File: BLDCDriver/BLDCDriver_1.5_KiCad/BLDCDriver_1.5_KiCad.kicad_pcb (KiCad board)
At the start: 2 copper layers, 42 x 43.2 mm, 53 parts, among them IC1 STSPIN32G4, J2 Debug, J3 Motor Out, J4 POWER, J5 CAN, SW1 SW_Push, U4 MCP2562-E-SN, U5 AS5048A-HTSP-500

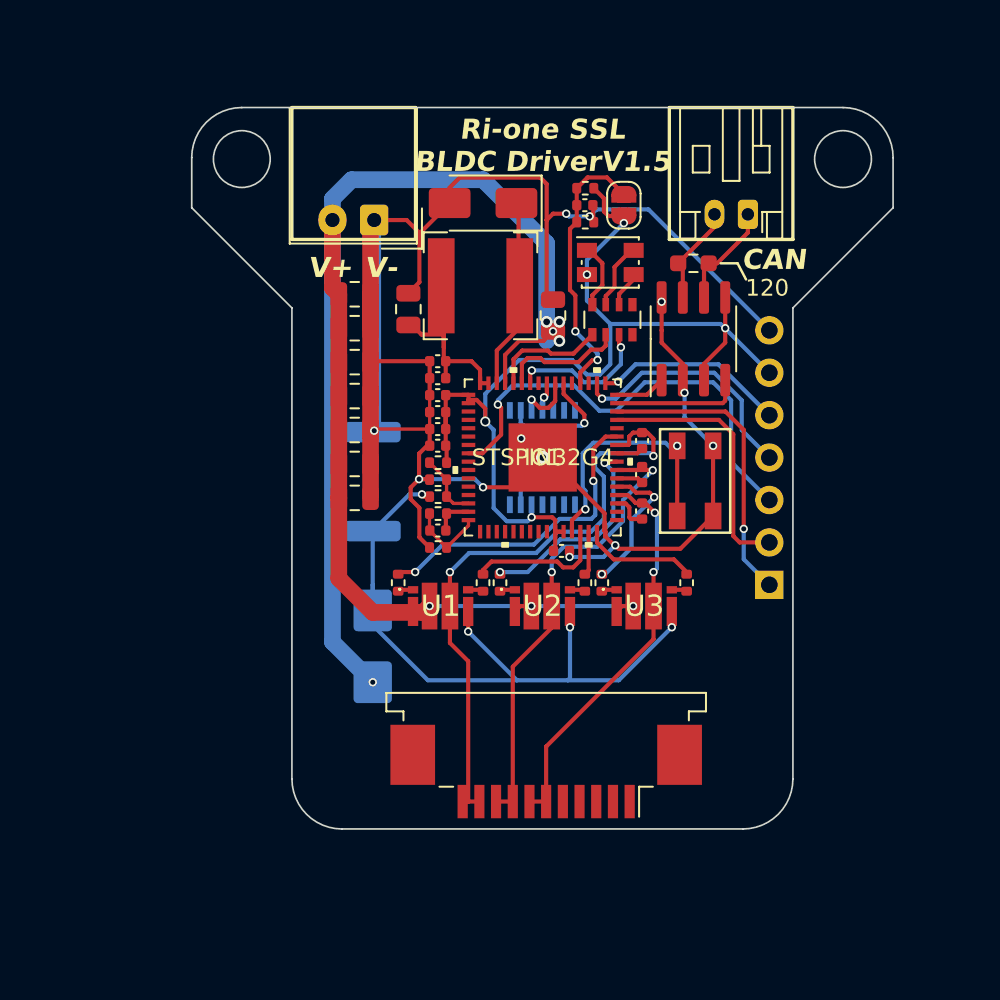
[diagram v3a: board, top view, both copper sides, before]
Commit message: ✨パワーラインのアートワークを仕上げた
[-] GNDビア
[-] CAN用LDO
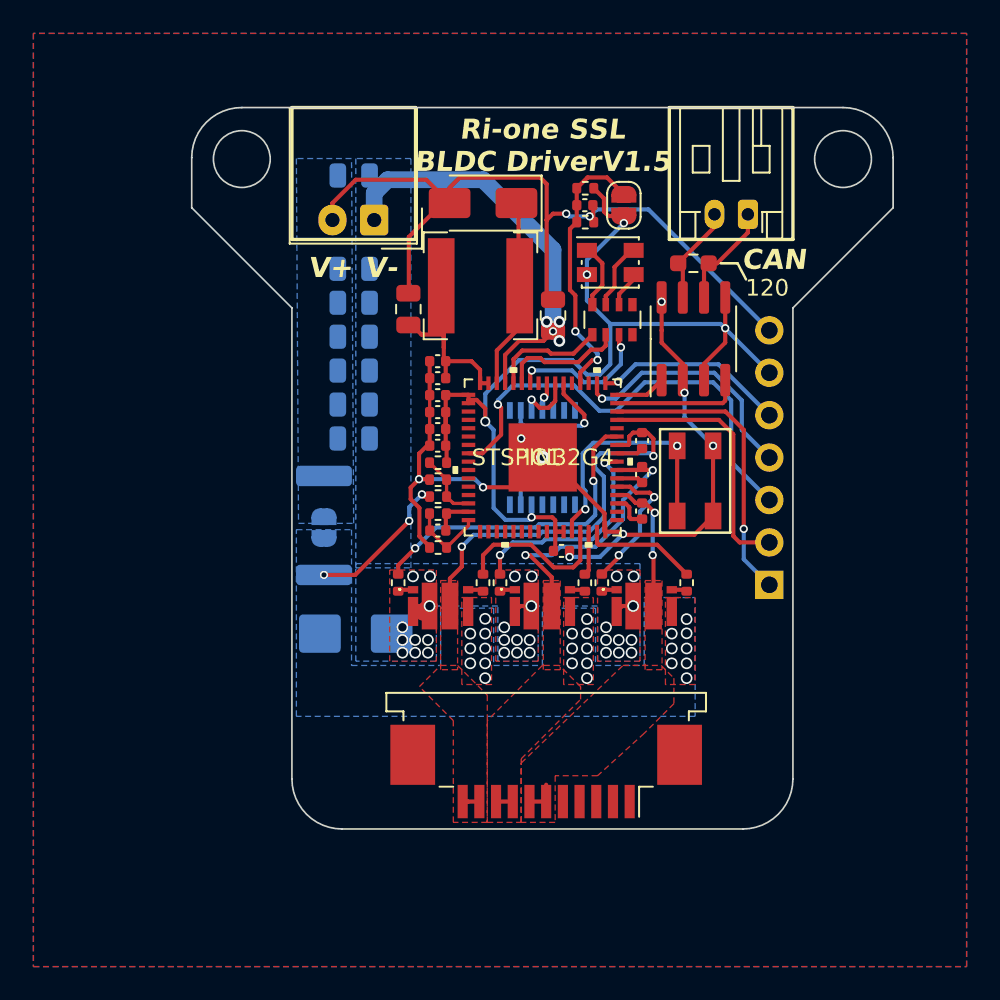
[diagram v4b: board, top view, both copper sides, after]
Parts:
- added JP2: Jumper_2_Open, Jumper:SolderJumper-2_P1.3mm_Open_RoundedPad1.0x1.5mm, B.Cu at (-13.1, 4.19)
- C1, C17, C18, C19, C2, C20, C9: moved to B.Cu
- moved C17 7.62 mm to (-11.3, -11.3), turned to 0 degrees
- moved C9 7.62 mm to (-11.3, -9.27), turned to 0 degrees
- moved C2 7.62 mm to (-11.3, -7.24), turned to 0 degrees
- moved C1 7.62 mm to (-11.3, -5.21), turned to 0 degrees
- moved C20 7.11 mm to (-11.3, -16.9), turned to 0 degrees
- moved C19 6.60 mm to (-11.3, -1.14), turned to 0 degrees
- moved R10 3.93 mm to (-13.1, 4.06)
- moved C18 2.54 mm to (-11.3, -3.17), turned to 0 degrees
- moved TVS1 1.27 mm to (-11.2, 10.5), turned to 180 degrees
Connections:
- J3 pad MP: unconnected-(J3-MountPin-PadMP) -> GND
- J4 pad 1: GND -> VD
- J4 pad 2: VD -> GND
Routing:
- net VD: track 99.4 -> 28.6 mm, vias 8 -> 34
- net SHUNT_P1: track 42.6 -> 8.86 mm, vias 4 -> 27
- net GND: track 139.6 -> 106.8 mm, vias 12 -> 11
- net OUT3: track 23.8 -> 10.4 mm
- net OUT1: track 37.2 -> 25.4 mm
- net OUT2: track 28.5 -> 18.2 mm
- net GLS1: track 8.32 -> 9.68 mm
- net GHS2: track 12.5 -> 13.1 mm
- added copper zone on B.Cu, net GND
- added copper zone on F.Cu, net GND
- added copper zone on F.Cu, net OUT1
- added copper zone on F.Cu, net OUT2
- added copper zone on F.Cu, net OUT3
- added copper zone on B.Cu, net SHUNT_P1
- added copper zone on F.Cu, net SHUNT_P1
- added copper zone on B.Cu, net VD
- added copper zone on F.Cu, net VD

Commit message: ✨ LED、LDO、ビアをやった
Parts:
- added C21: 100nF, Capacitor_SMD:C_0402_1005Metric, F.Cu at (6.86, -18.7)
- added C22: 100nF, Capacitor_SMD:C_0402_1005Metric, F.Cu at (2.03, -18.7)
- added C23: 100nF, Capacitor_SMD:C_0402_1005Metric, F.Cu at (5.59, -5.36)
- added D3: LED, LED_SMD:LED_0603_1608Metric_Pad1.05x0.95mm_HandSolder, F.Cu at (-4.32, -19.0)
- added D4: LED, LED_SMD:LED_0603_1608Metric_Pad1.05x0.95mm_HandSolder, F.Cu at (-2.69, -19.0)
- added D5: LED, LED_SMD:LED_0603_1608Metric_Pad1.05x0.95mm_HandSolder, F.Cu at (0.10, -19.0)
- added R11: 10k, Resistor_SMD:R_0402_1005Metric, F.Cu at (-5.69, -18.3)
- added R17: 1k, Resistor_SMD:R_0402_1005Metric, F.Cu at (-1.37, -18.3)
- added R18: 1k, Resistor_SMD:R_0402_1005Metric, F.Cu at (1.14, -15.5)
- added U6: AP7375-50SA, BLDC:AP7375-33SA-7_DIO, F.Cu at (4.45, -18.7)
- moved D1 0.25 mm to (-3.56, -15.5)
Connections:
- IC1 pad 53: unconnected-(IC1-PD2-Pad53) -> LED_Alive
- U4 pad 3: VDD -> +5V
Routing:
- net GND: track 106.8 -> 79.6 mm, vias 11 -> 44
- net VCC: track 12.4 -> 37.8 mm, vias 0 -> 2
- net +5V: track 0.00 -> 20.2 mm, vias 0 -> 2
- net VD: track 28.6 -> 10.0 mm, vias 34 -> 35
- net LED_Alive: track 0.00 -> 11.6 mm, vias 0 -> 2
- net nRST: track 27.6 -> 24.0 mm
- net VDD: track 62.0 -> 64.8 mm, vias 5 -> 7
- net Net-(D5-A): track 0.00 -> 2.55 mm, vias 0 -> 2
- net Net-(D3-A): track 0.00 -> 1.65 mm
- net Net-(D4-A): track 0.00 -> 1.60 mm
- net SWCLK: track 14.9 -> 13.8 mm
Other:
- board text added: "VIN"

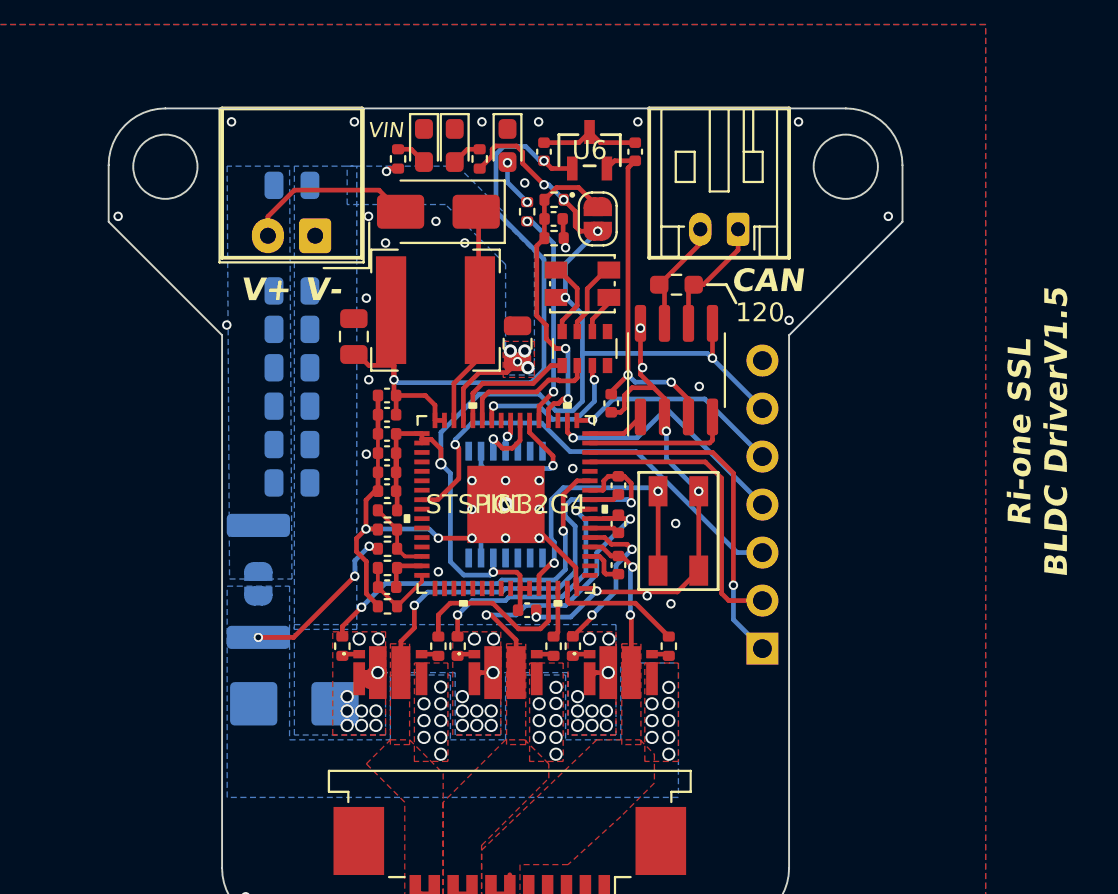
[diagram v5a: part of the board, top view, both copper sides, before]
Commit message: ✨ID切り替えパッド、GNDベタ、パターン禁止エリア設定、テストポイント
次は抵抗値の決定などをしていきたい。
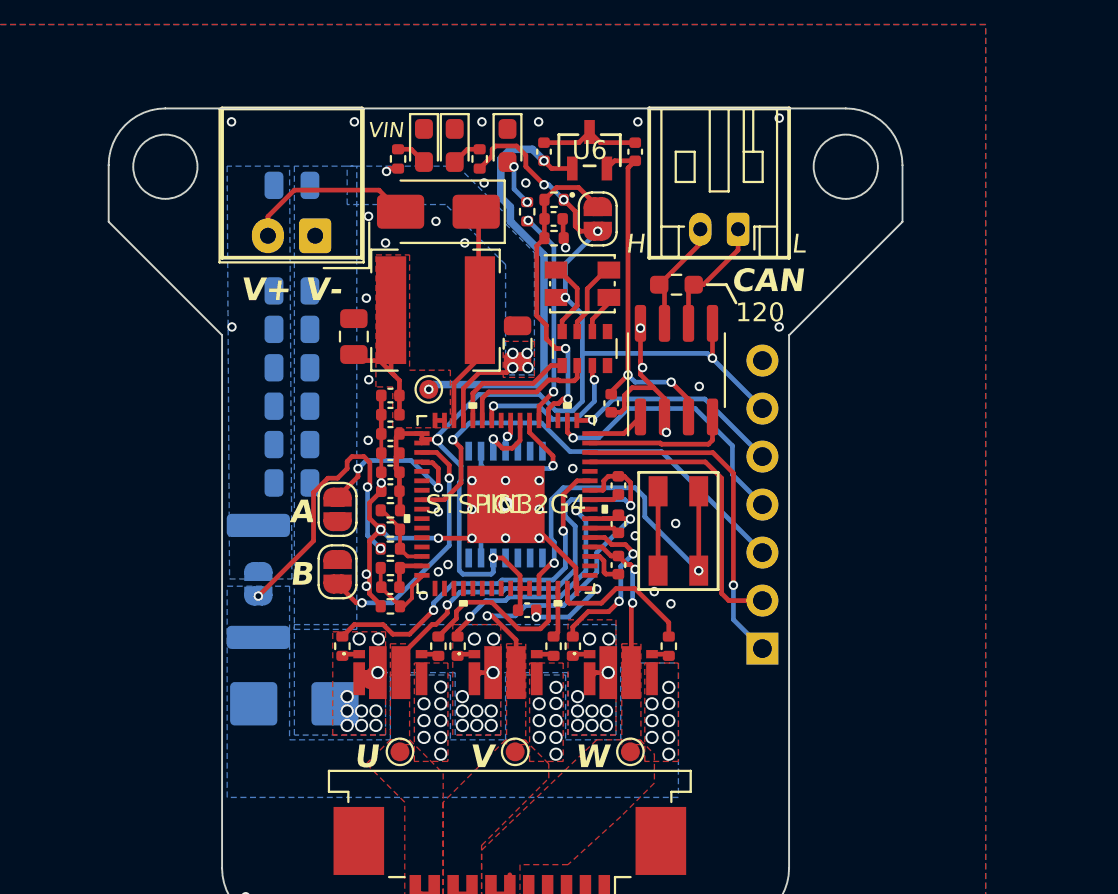
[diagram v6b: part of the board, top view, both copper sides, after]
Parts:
- removed C$1: 10uf 25v, Capacitor_SMD:C_0805_2012Metric
- added C24: 10uf 25v, Capacitor_SMD:C_0805_2012Metric, F.Cu at (-8.03, -8.89)
- added JP3: Jumper_2_Open, Jumper:SolderJumper-2_P1.3mm_Open_RoundedPad1.0x1.5mm, F.Cu at (-8.89, 3.56)
- added JP4: Jumper_2_Open, Jumper:SolderJumper-2_P1.3mm_Open_RoundedPad1.0x1.5mm, F.Cu at (-8.89, 0.25)
- added TP1: TestPoint_Small, TestPoint:TestPoint_Pad_D1.0mm, F.Cu at (-4.06, -6.10)
- added TP2: TestPoint_Small, TestPoint:TestPoint_Pad_D1.0mm, F.Cu at (-5.59, 13.1)
- added TP3: TestPoint_Small, TestPoint:TestPoint_Pad_D1.0mm, F.Cu at (0.51, 13.1)
- added TP4: TestPoint_Small, TestPoint:TestPoint_Pad_D1.0mm, F.Cu at (6.60, 13.1)
- C21: value 100nF -> 10uF
- C22: value 100nF -> 1uF
- D3: value LED -> LED_Blue
- D4: value LED -> LED_Green
- D5: value LED -> LED_White
- U6: value AP7375-50SA -> AP7375-33SA-7
- moved C3 0.18 mm to (-6.10, -0.71)
- moved C4 0.18 mm to (-6.10, -3.74)
- moved C5 0.18 mm to (-6.10, -1.71)
- moved C6 0.18 mm to (-6.10, -2.72)
- moved C7 0.18 mm to (-6.10, -5.77)
- moved C8 0.18 mm to (-6.10, -4.75)
- moved C16 0.17 mm to (-6.10, 4.37)
- moved R16 0.15 mm to (-6.10, 3.35)
- moved R12 0.15 mm to (-6.10, 2.34)
- moved R13 0.15 mm to (-6.10, 5.38)
- moved R14 0.15 mm to (-6.10, 0.30)
- moved R15 0.15 mm to (-6.10, 1.32)
- turned SW1 to 90 degrees
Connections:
- IC1 pad 3: unconnected-(IC1-PC13-Pad3) -> SWA
- IC1 pad 4: unconnected-(IC1-PC14-Pad4) -> SWB
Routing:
- net SWA: track 0.00 -> 13.6 mm, vias 0 -> 2
- net GND: track 79.6 -> 68.6 mm, vias 44 -> 49
- net SWB: track 0.00 -> 9.02 mm, vias 0 -> 2
- net SHUNT_P1: track 8.86 -> 15.7 mm
- net VCC: track 37.8 -> 32.3 mm
- net SW: track 15.4 -> 19.9 mm
- net GLS3: track 6.82 -> 7.90 mm
- net SWCLK: track 13.8 -> 14.7 mm
- net VDD: track 64.8 -> 64.0 mm
- net OUT1: track 25.4 -> 24.7 mm
- net GHS3: track 8.40 -> 9.03 mm
- added copper zone on F.Cu, net VCC
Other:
- board text added: "A"
- board text added: "B"
- board text added: "BLDC Driver V1.5"
- board text added: "CH"
- board text added: "CL"
- board text added: "H"
- board text added: "L"
- board text added: "U"
- board text added: "V"
- board text added: "W"
- board text removed: "Ri-one SSL BLDC DriverV1.5"
